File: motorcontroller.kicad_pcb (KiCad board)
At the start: 4 copper layers, 110 x 160 mm, 176 parts, among them J101 TYPE-C-31-M-12, J102 STLink_02x05, J103 STRLCK, J104 IGN, J105 THROTTLE, J106 UART, J107 IO, J108 DIR, J109 EN, J110 CAN, J201 FUSE, Q101 AP2300, Q401 STP15810, Q402 STP15810, Q403 STP15810, Q404 STP15810, Q405 STP15810, Q406 STP15810, Q407 STP15810, Q408 STP15810, Q409 STP15810, Q410 STP15810, Q411 STP15810, Q412 STP15810, Q501 WSP6946, Q502 WSP6946, SW301 SW_Push, U101 SN65HVD231DR, U201 LM2596HVGT-ADJ, U202 XL1509-3.3E1, U203 STM32F103C8Tx, U301 M95640-WMN6TP, U401 LM5110-1MX, U402 LM5110-1MX, U403 LM5110-1MX, U404 LM5110-1MX, U405 LM5110-1MX, U406 LM5110-1MX, Y301 12MHz

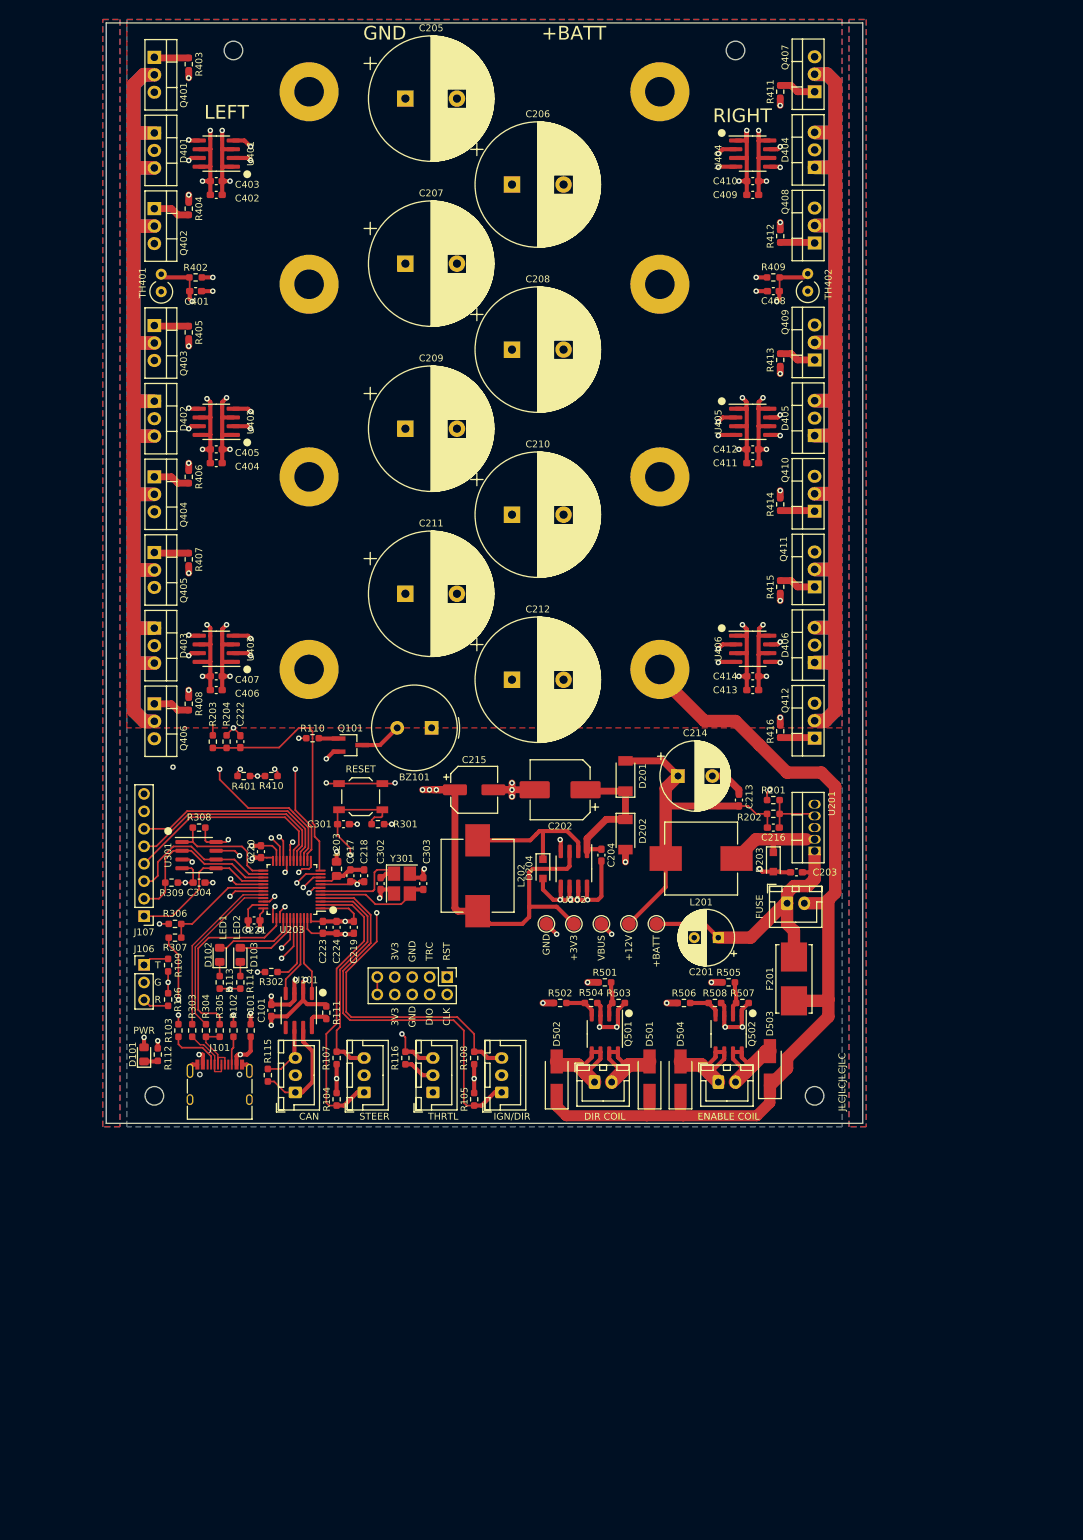
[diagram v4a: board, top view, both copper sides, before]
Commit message: M3 mounting holes
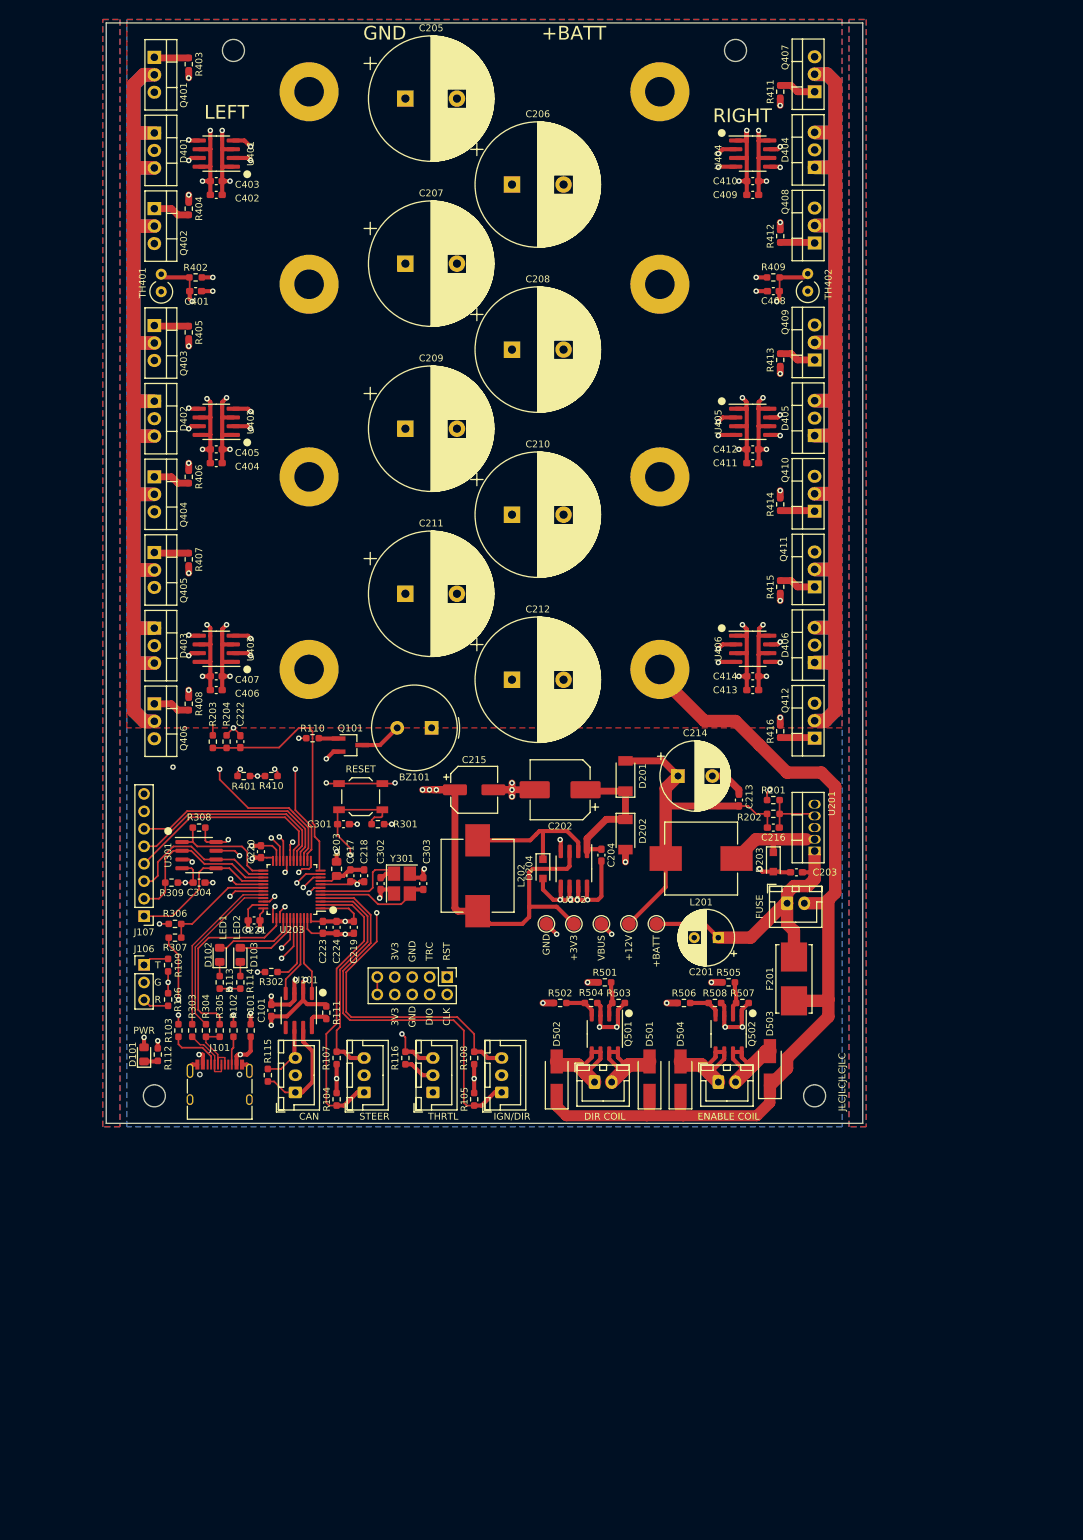
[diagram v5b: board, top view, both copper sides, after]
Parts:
- D401, D402, D403, D404, D405, D406: value G30C120CTW -> G40C100CTFW
- H101, H102, H103, H104: footprint MountingHole:MountingHole_2.7mm_M2.5 -> MountingHole:MountingHole_3.2mm_M3

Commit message: Tweak PCB and add gerbers
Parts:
- added C102: 4.7nF, Capacitor_SMD:C_0603_1608Metric_Pad1.08x0.95mm_HandSolder, F.Cu at (53.8, 170.8)
- added D104: NUP2105L, Package_TO_SOT_SMD:SOT-23, F.Cu at (48.8, 175.0)
- added D105: PRTR5V0U2X, Package_TO_SOT_SMD:SOT-143, F.Cu at (41.0, 171.8)
- added R117: 10k, Resistor_SMD:R_0603_1608Metric_Pad0.98x0.95mm_HandSolder, F.Cu at (55.0, 130.8)
- added R118: 60R, Resistor_SMD:R_0603_1608Metric_Pad0.98x0.95mm_HandSolder, F.Cu at (52.2, 169.2)
- added R119: 22R, Resistor_SMD:R_0603_1608Metric_Pad0.98x0.95mm_HandSolder, F.Cu at (47.8, 157.5)
- added R120: 22R, Resistor_SMD:R_0603_1608Metric_Pad0.98x0.95mm_HandSolder, F.Cu at (46.0, 157.5)
- added R121: 22R, Resistor_SMD:R_0603_1608Metric_Pad0.98x0.95mm_HandSolder, F.Cu at (56.8, 157.5)
- added R122: 22R, Resistor_SMD:R_0603_1608Metric_Pad0.98x0.95mm_HandSolder, F.Cu at (51.2, 157.5)
- added R205: 0R, Resistor_SMD:R_0603_1608Metric_Pad0.98x0.95mm_HandSolder, F.Cu at (76.5, 138.8)
- added R206: 0R, Resistor_SMD:R_0603_1608Metric_Pad0.98x0.95mm_HandSolder, F.Cu at (103.5, 132.2)
- added R310: 22R, Resistor_SMD:R_0603_1608Metric_Pad0.98x0.95mm_HandSolder, F.Cu at (44.8, 143.0)
- added R311: 22R, Resistor_SMD:R_0603_1608Metric_Pad0.98x0.95mm_HandSolder, F.Cu at (44.8, 146.5)
- added R312: 22R, Resistor_SMD:R_0603_1608Metric_Pad0.98x0.95mm_HandSolder, F.Cu at (44.8, 144.8)
- C205, C206, C207, C208, C209, C210, C211, C212: footprint Capacitor_THT:CP_Radial_D18.0mm_P7.50mm -> GozLib:CP_Radial_D18.0mm_P7.50mm_P5.00mm
- J101: footprint Connector_USB:USB_C_Receptacle_HRO_TYPE-C-31-M-12 -> GozLib:USB_C_Receptacle_HRO_TYPE-C-31-M-12_Handsoldering
- L202: footprint GozLib:L_10.4x10.4_H4.8_Handsoldering -> GozLib:L_YNR6045
- R115: value 120R -> 60R
- R308, R309, R503, R504, R507, R508: value 62k -> 10k
- SW301: footprint Button_Switch_SMD:SW_SPST_TL3342 -> GozLib:SW_SPST_TS-1185EC
- Y301: value 12MHz -> 8MHz; footprint Crystal:Crystal_SMD_3225-4Pin_3.2x2.5mm_HandSoldering -> Crystal:Crystal_SMD_5032-2Pin_5.0x3.2mm_HandSoldering
- moved C215 15.6 mm to (80.0, 152.0)
- moved J105 11.5 mm to (84.0, 180.5)
- moved R116 11.5 mm to (80.0, 175.5)
- moved R115 11.4 mm to (55.8, 169.2), turned to 180 degrees
- moved C101 9.94 mm to (54.0, 160.0), turned to 180 degrees
- moved C302 8.65 mm to (68.4, 142.2)
- moved J104 8.53 mm to (74.0, 180.5)
- moved R105 8.53 mm to (70.0, 181.5)
- moved R108 8.53 mm to (70.0, 175.5)
- moved C217 7.56 mm to (60.9, 141.4)
- moved C218 7.55 mm to (62.4, 141.4)
- moved L203 6.56 mm to (59.2, 141.5)
- moved Y301 5.86 mm to (65.7, 144.8)
- moved L202 5.64 mm to (80.2, 143.5), turned to 180 degrees
- moved R302 5.52 mm to (49.5, 157.5), turned to -90 degrees
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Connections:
- C213 pad 1: +12V -> Net-(C213-Pad1)
- C214 pad 1: +12V -> Net-(C213-Pad1)
- C215 pad 1: +3V3 -> Net-(C215-Pad1)
- C216 pad 2: +12V -> Net-(C213-Pad1)
- J106 pad 1: /MCU/UART_TX -> Net-(J106-Pad1)
- J106 pad 3: /MCU/UART_RX -> Net-(J106-Pad3)
- J110 pad 1: Net-(J110-Pad1) -> Net-(D104-Pad2)
- J110 pad 3: Net-(J110-Pad3) -> Net-(D104-Pad1)
- L201 pad 2: +12V -> Net-(C213-Pad1)
- L202 pad 2: +3V3 -> Net-(C215-Pad1)
- R106 pad 2: /MCU/UART_RX -> Net-(J106-Pad3)
- R109 pad 2: /MCU/UART_TX -> Net-(J106-Pad1)
- R115 pad 1: Net-(J110-Pad1) -> Net-(D104-Pad1)
- R115 pad 2: Net-(J110-Pad3) -> Net-(C102-Pad1)
- R202 pad 2: +12V -> Net-(C213-Pad1)
- TP203 pad 1: +3V3 -> Net-(C215-Pad1)
- TP204 pad 1: +12V -> Net-(C213-Pad1)
- U101 pad 1: /MCU/CAN_TX -> Net-(R121-Pad2)
- U101 pad 4: /MCU/CAN_RX -> Net-(R122-Pad1)
- U101 pad 5: unconnected-(U101-Pad5) -> Net-(C102-Pad1)
- U101 pad 6: Net-(J110-Pad3) -> Net-(D104-Pad2)
- U101 pad 7: Net-(J110-Pad1) -> Net-(D104-Pad1)
- U202 pad 3: +3V3 -> Net-(C215-Pad1)
- U203 pad 21: /MCU/ENABLE_LEFT -> /MCU/ENABLE_RIGHT
- U203 pad 22: /MCU/ENABLE_RIGHT -> /MCU/ENABLE_LEFT
- U203 pad 26: /MCU/SCK -> Net-(R310-Pad2)
- U203 pad 27: /MCU/MISO -> Net-(R312-Pad2)
- U203 pad 28: /MCU/MOSI -> Net-(R311-Pad2)
- Y301 pad 2: GND -> Net-(C303-Pad1)
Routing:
- net +12V: track 173.0 -> 109.0 mm, vias 12 -> 15
- net +3V3: track 304.0 -> 242.2 mm, vias 17 -> 16
- net Net-(C215-Pad1): track 0.00 -> 49.0 mm
- net Net-(C213-Pad1): track 0.00 -> 46.0 mm
- net Net-(J106-Pad3): track 0.00 -> 27.4 mm, vias 0 -> 1
- net Net-(J106-Pad1): track 0.00 -> 24.6 mm, vias 0 -> 1
- net /MCU/UART_RX: track 32.9 -> 9.91 mm, vias 1 -> 0
- net Net-(D104-Pad2): track 0.00 -> 21.2 mm
- net Net-(D104-Pad1): track 0.00 -> 19.0 mm
- net /MCU/UART_TX: track 29.7 -> 11.8 mm, vias 1 -> 0
- net /MCU/THROTTLE: track 46.6 -> 64.5 mm
- net Net-(J110-Pad1): track 17.1 -> 0.00 mm
- net /MCU/IGNITION: track 61.5 -> 45.6 mm
- net /MCU/ENABLE_LEFT: track 79.1 -> 90.9 mm
- net /MCU/PWM_LEFT: track 138.2 -> 126.8 mm
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- added copper zone on F.Cu, net GND
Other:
- board text added: "1"
- board text added: "2"
- board text added: "3"
- board text added: ":D"
- board text added: "CK"
- board text added: "DI"
- board text added: "DO"
- board text added: "Motor Controller V1"
